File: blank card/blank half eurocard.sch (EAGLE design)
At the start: 1 part, among them J1 8-1393644-0

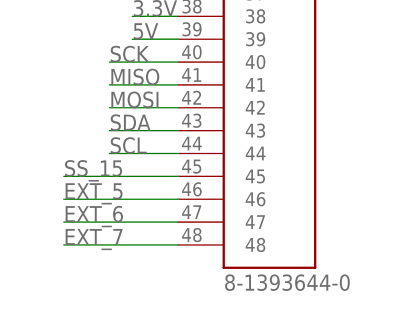
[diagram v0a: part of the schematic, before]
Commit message: fixed library attributes for the din41612 connector, fixed git problems
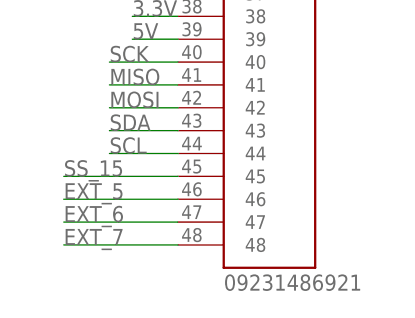
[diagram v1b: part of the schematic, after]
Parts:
- J1: value 8-1393644-0 -> 09231486921; device 8-1393644-0:8-1393644-0 -> din41612_48_pin_board:09231486921
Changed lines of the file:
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@@
 </classes>
 <parts>
-<part name="J1" library="8-1393644-0" deviceset="8-1393644-0" device=""/>
+<part name="J1" library="din41612_48_pin_board" deviceset="09231486921" device=""/>
 <part name="GND1" library="supply1" library_urn="urn:adsk.eagle:library:371" deviceset="GND" device=""/>
 <part name="GND2" library="supply1" library_urn="urn:adsk.eagle:library:371" deviceset="GND" device=""/>
